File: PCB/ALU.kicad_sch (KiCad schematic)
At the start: 30 parts, among them U10 74LS08, U11 74LS02, U12 74LS173, U13 74LS283, U14 74LS283, U15 74LS86, U16 74LS86, U17 74LS245

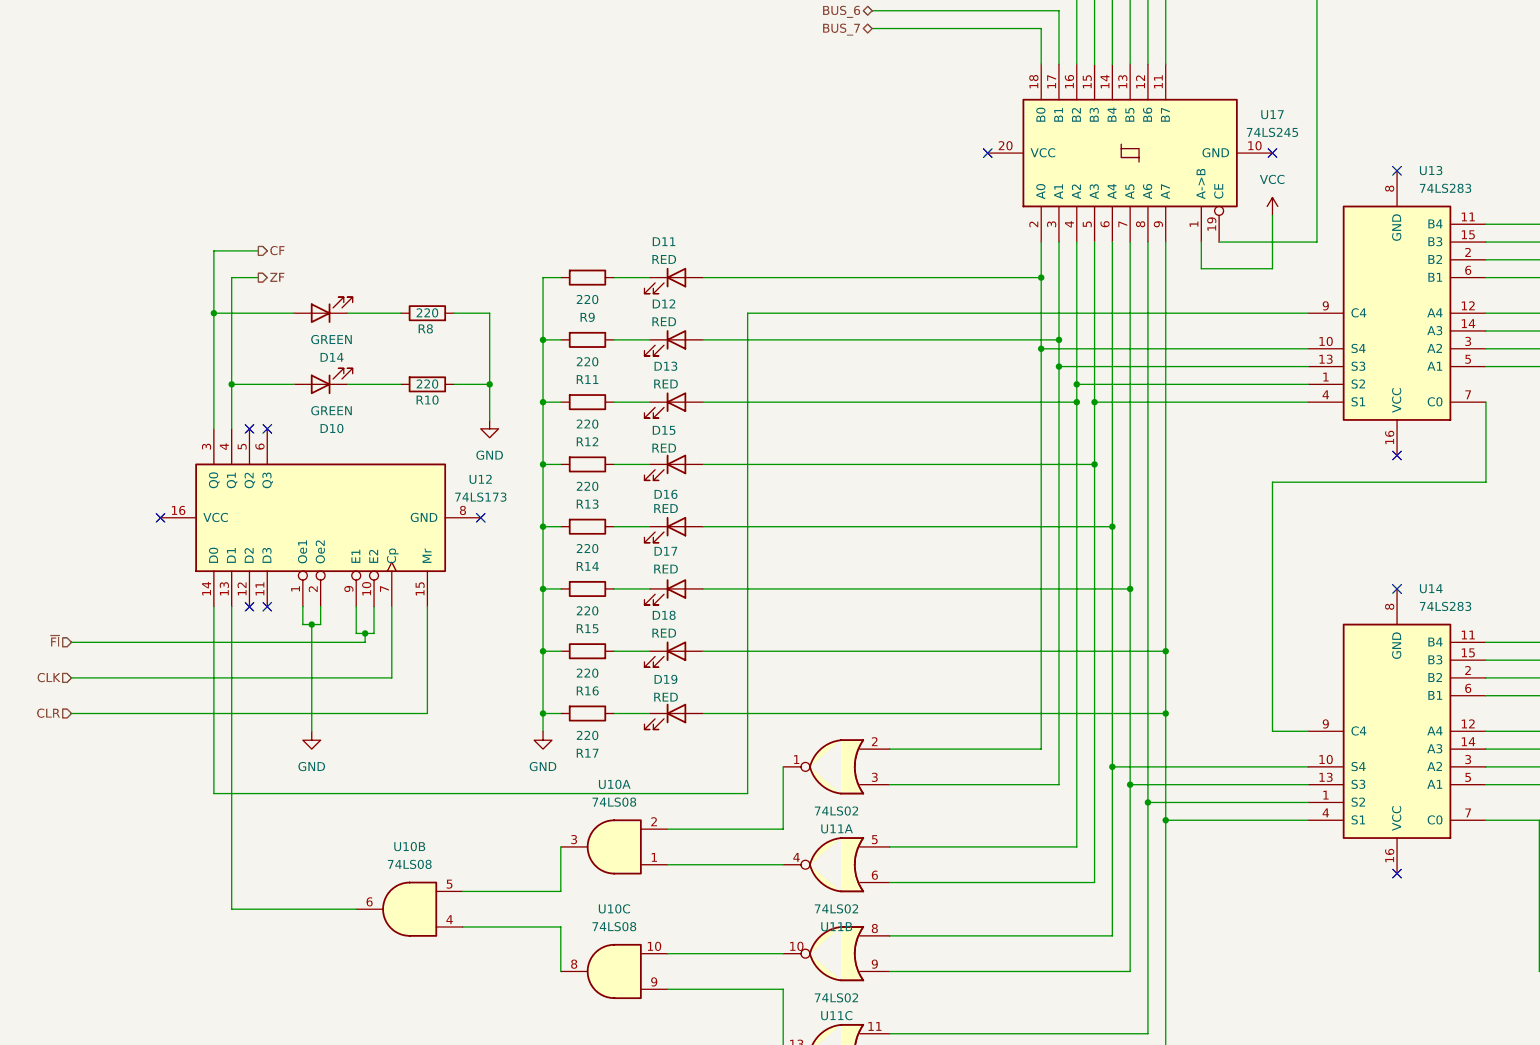
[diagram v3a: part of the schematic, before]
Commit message: Routed the traces for the ground
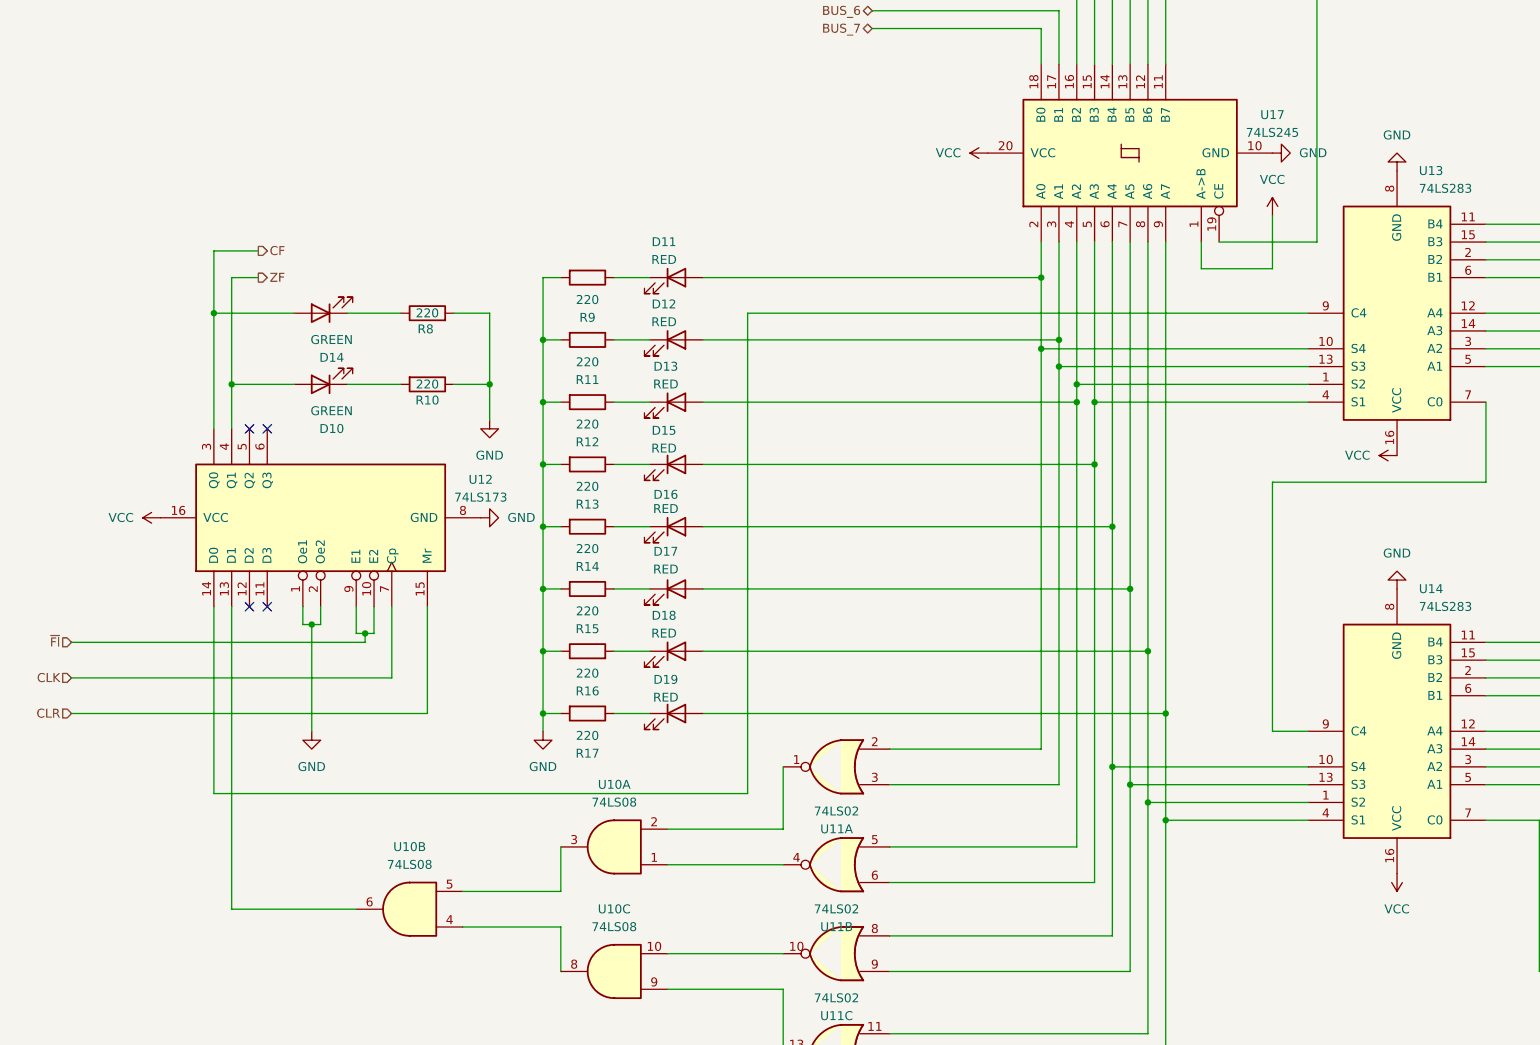
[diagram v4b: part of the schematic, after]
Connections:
- net GND: now also U12.8 (GND), U13.8 (GND), U14.8 (GND), U17.10 (GND)
- net VCC: now also U12.16 (VCC), U13.16 (VCC), U14.16 (VCC), U17.20 (VCC)
- net at U11.11, U14.1 (S2), U17.8 (A6): now also D18.2 (A)
- net at D19.2 (A), U11.12, U14.4 (S1)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: no longer D18.2 (A)
- no-connect marks 15 -> 7

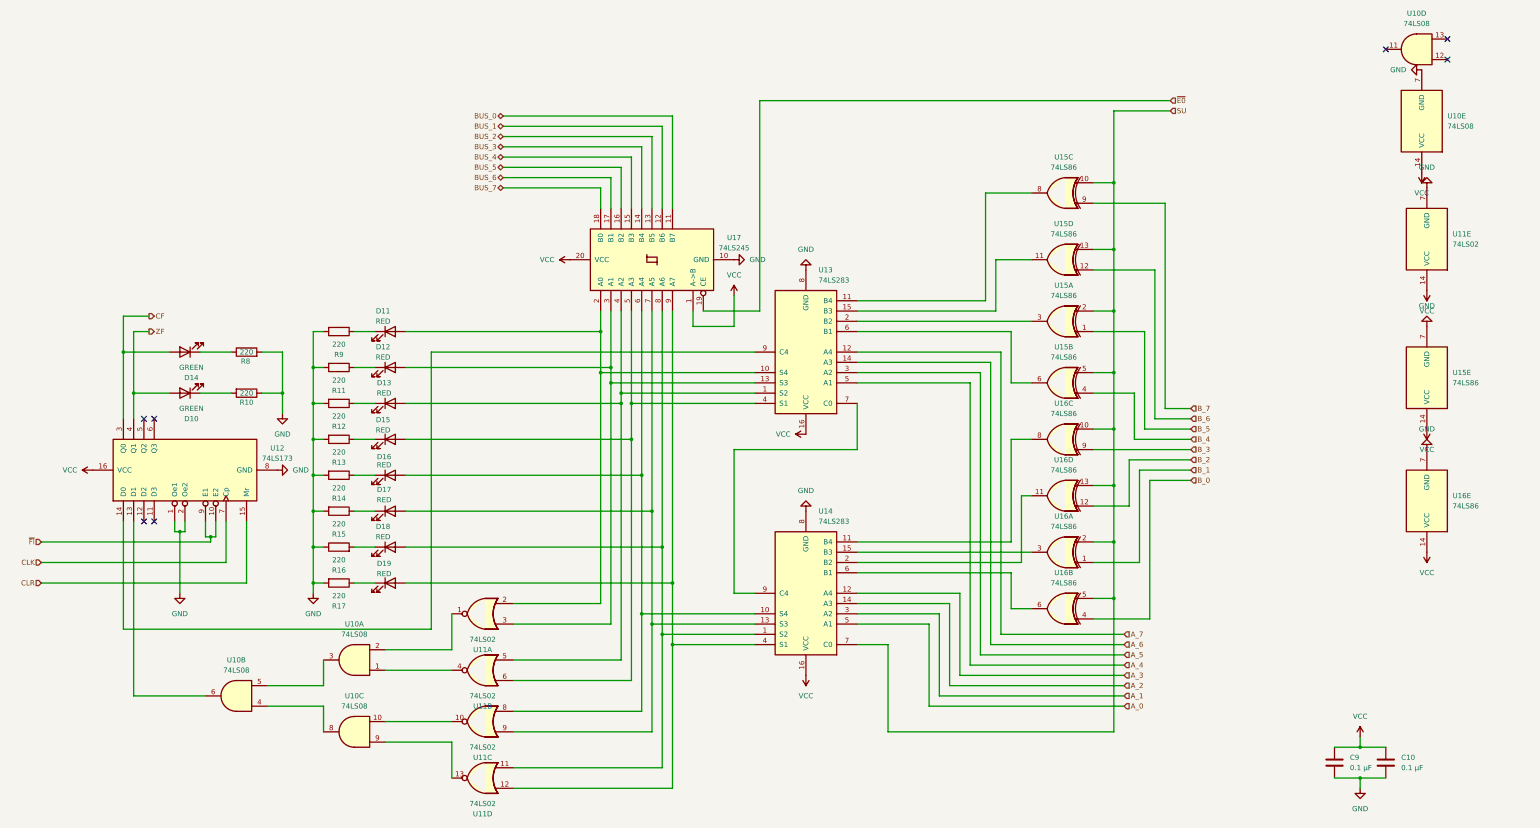
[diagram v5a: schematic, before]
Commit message: Add decupling caps and reroute pcb. Updated BOM to match new number of caps
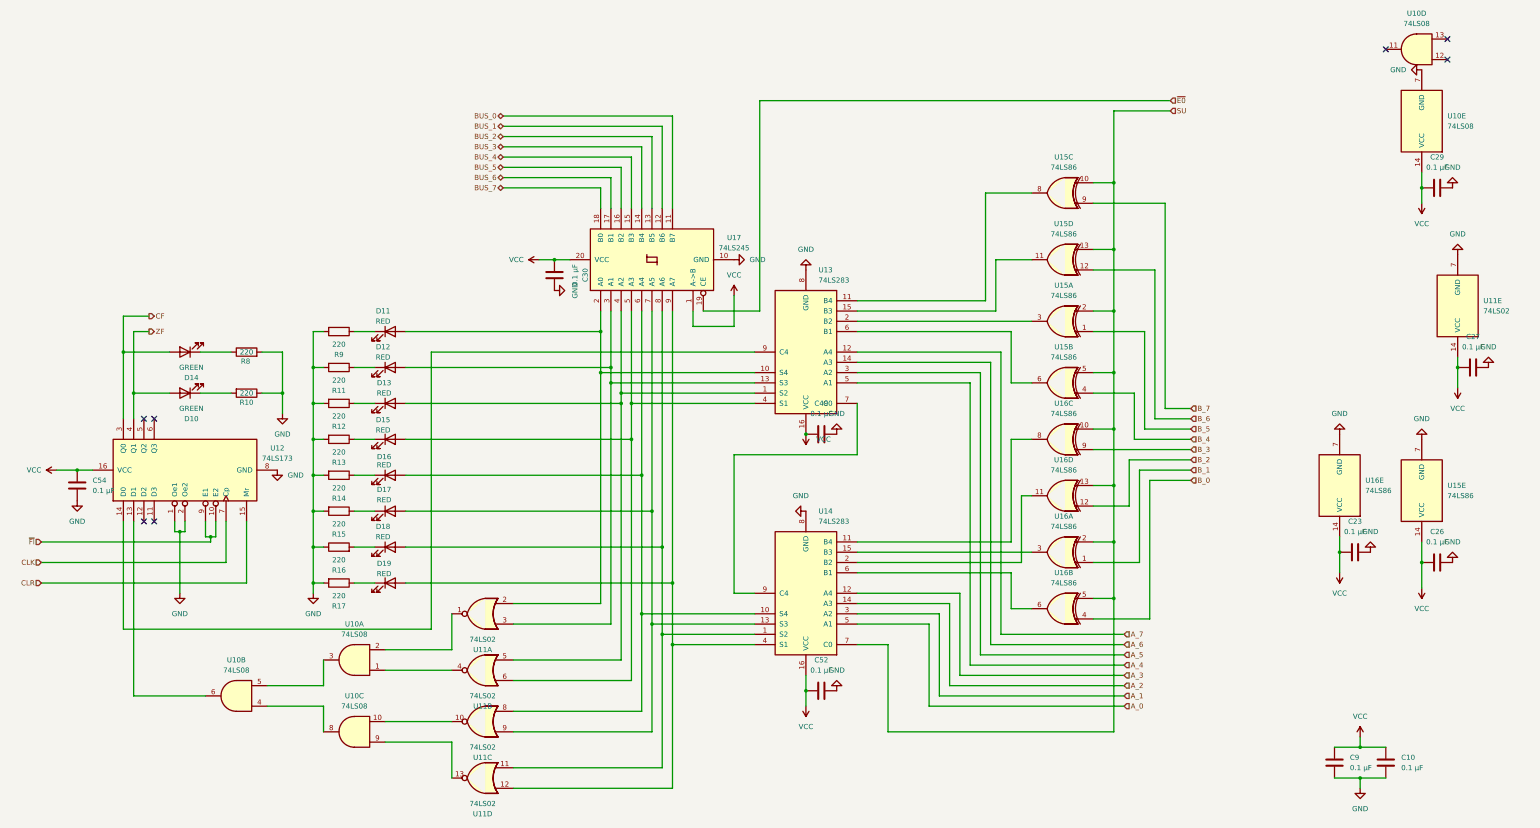
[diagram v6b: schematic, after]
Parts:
- added C23, C26, C27, C29, C30, C49, C52, C54: 0.1 µF, Capacitor_THT:C_Radial_D5.0mm_H5.0mm_P2.00mm, symbol Device:C
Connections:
- net GND: now also C23.2, C26.2, C27.2, C29.2, C30.2, C49.2, C52.2, C54.1
- net VCC: now also C23.1, C26.1, C27.1, C29.1, C30.1, C49.1, C52.1, C54.2
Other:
- moved on the sheet: U11E, U15E, U16E

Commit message: Redoing PCB layout and fixed some signal flow convention errors
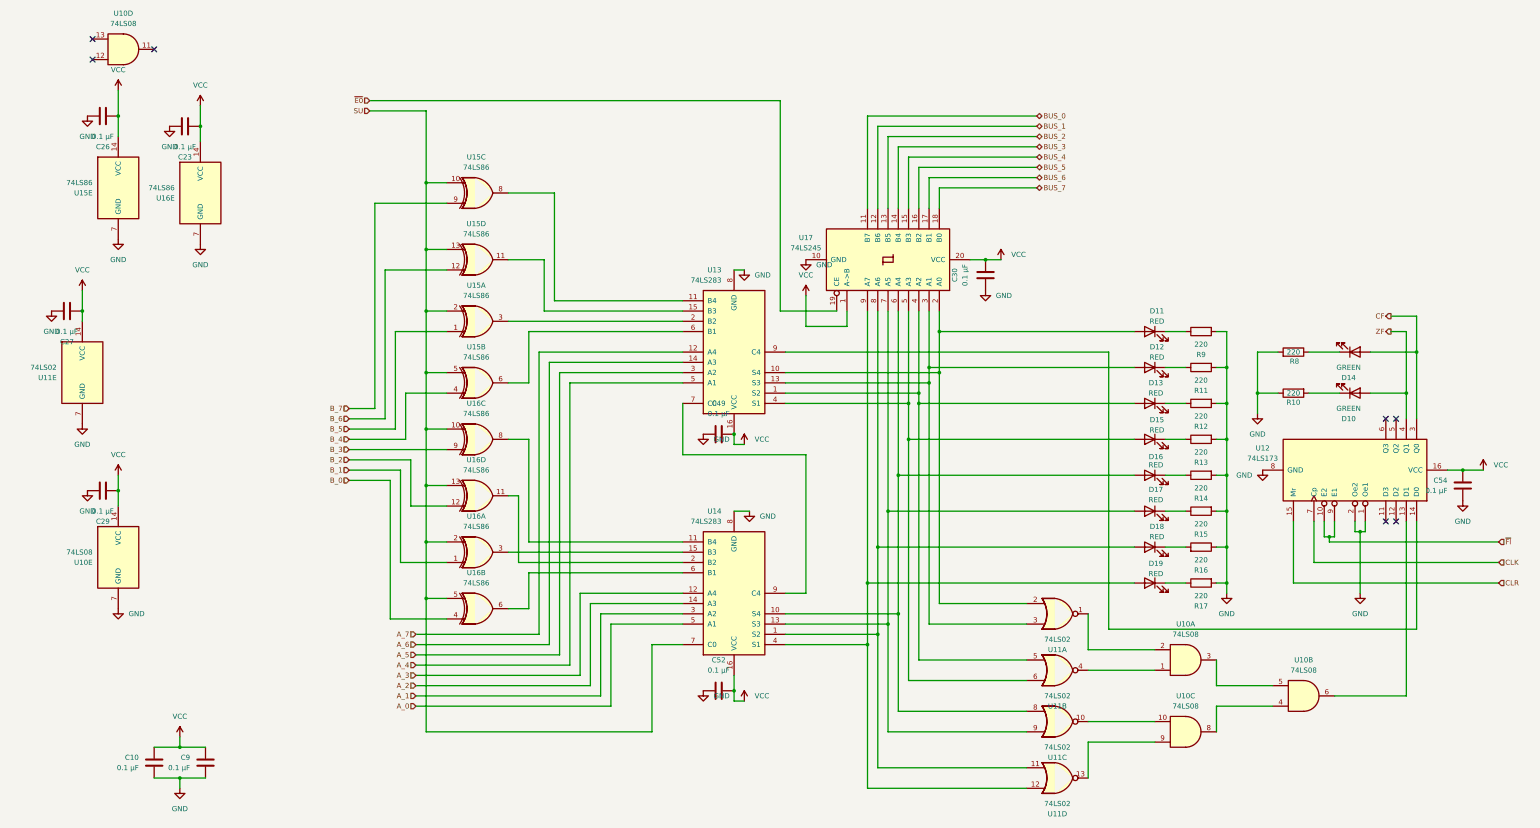
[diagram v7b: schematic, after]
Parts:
- U11, U15: footprint footprints:N14 -> Custom:N14
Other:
- moved on the sheet: C10, C23, C26, C27, C29, C30, C49, C52, C54, C9, D10, D11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
